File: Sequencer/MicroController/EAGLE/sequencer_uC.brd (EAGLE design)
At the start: 70 x 70 mm, 29 parts, among them J1 AVR_SPI_PROG_3X2NS, Q1 16MHz

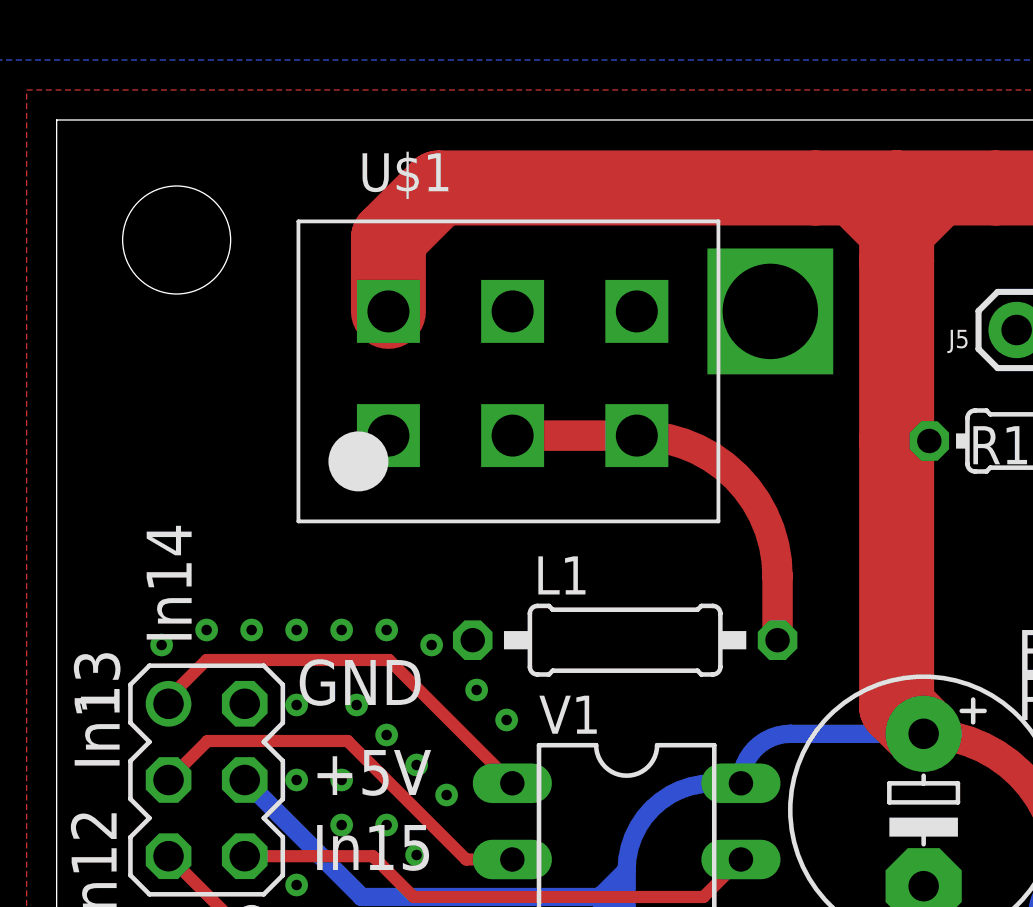
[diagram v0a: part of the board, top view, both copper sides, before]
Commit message: fixed TE pinout
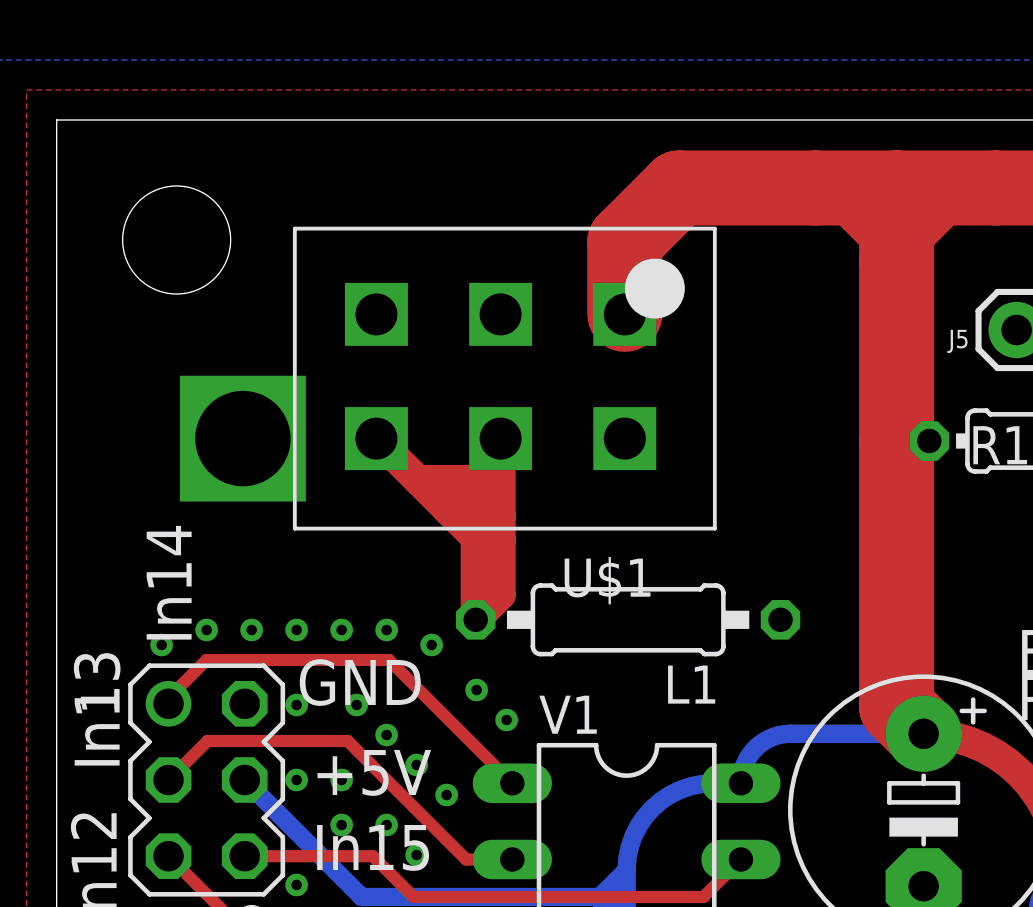
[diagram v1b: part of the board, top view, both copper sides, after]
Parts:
- moved U$1 8.95 mm to (18.9, 59.4), turned to 180 degrees
- moved L1 0.69 mm to (19.1, 53.3), turned to 180 degrees
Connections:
- net +5V: now also U$1.NULL
- net DGND: no longer U$1.NULL
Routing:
- net AGND: track 12.9 -> 22.7 mm
- net +5V: track 314.2 -> 306.4 mm
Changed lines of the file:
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@@
 <?xml version="1.0" encoding="utf-8"?>
 <!DOCTYPE eagle SYSTEM "eagle.dtd">
-<eagle version="9.3.1">
+<eagle version="9.2.2">
 <drawing>
 <settings>
@@
 <attribute name="VALUE" x="52.46" y="35.079" size="1.27" layer="27" ratio="10"/>
 </element>
-<element name="L1" library="rcl" library_urn="urn:adsk.eagle:library:334" package="0207/10" package3d_urn="urn:adsk.eagle:package:23491/2" value="47uH" x="18.95" y="52.66" smashed="yes">
-<attribute name="NAME" x="15.902" y="54.184" size="1.27" layer="25" ratio="10"/>
-<attribute name="SPICEPREFIX" value="L" x="38" y="-21" size="1.778" layer="27" display="off"/>
-<attribute name="VALUE" x="16.6894" y="52.025" size="1.27" layer="27" ratio="10"/>
+<element name="L1" library="rcl" library_urn="urn:adsk.eagle:library:334" package="0207/10" package3d_urn="urn:adsk.eagle:package:23491/1" value="47uH" x="19.05" y="53.34" smashed="yes" rot="R180">
+<attribute name="NAME" x="22.098" y="51.816" size="1.27" layer="25" ratio="10" rot="R180"/>
+<attribute name="SPICEPREFIX" value="L" x="0" y="127" size="1.778" layer="27" rot="R180" display="off"/>
+<attribute name="VALUE" x="21.3106" y="53.975" size="1.27" layer="27" ratio="10" rot="R180"/>
 </element>
 <element name="Q1" library="special" library_urn="urn:adsk.eagle:library:367" package="QS" package3d_urn="urn:adsk.eagle:package:26647/2" value="16MHz" x="29" y="27" smashed="yes" rot="R90">
@@
 <attribute name="VALUE" x="31.78" y="34.137" size="1.27" layer="27" ratio="10" rot="R180"/>
 </element>
-<element name="R1" library="resistor" library_urn="urn:adsk.eagle:library:348" package="0204/7" package3d_urn="urn:adsk.eagle:package:23498/1" value="10k" x="32.9" y="59.3" smashed="yes" rot="R180">
+<element name="R1" library="resistor" library_urn="urn:adsk.eagle:library:348" package="0204/7" package3d_urn="urn:adsk.eagle:package:25945/1" value="10k" x="32.9" y="59.3" smashed="yes" rot="R180">
 <attribute name="NAME" x="32.491" y="59.795" size="1.27" layer="25" ratio="10" rot="R180"/>
 <attribute name="VALUE" x="35.475" y="59.7858" size="1.27" layer="27" ratio="10" rot="R180"/>
 </element>
-<element name="R2" library="rcl" library_urn="urn:adsk.eagle:library:334" package="0204/7" package3d_urn="urn:adsk.eagle:package:23498/2" value="10k" x="53" y="54" smashed="yes" rot="R90">
+<element name="R2" library="rcl" library_urn="urn:adsk.eagle:library:334" package="0204/7" package3d_urn="urn:adsk.eagle:package:23498/1" value="10k" x="53" y="54" smashed="yes" rot="R90">
 <attribute name="NAME" x="51.7046" y="51.46" size="0.9906" layer="25" ratio="10" rot="R90"/>
 <attribute name="SPICEPREFIX" value="R" x="126.66" y="84.48" size="1.778" layer="27" rot="R90" display="off"/>
 <attribute name="VALUE" x="55.4826" y="54.3744" size="0.9906" layer="27" ratio="10" rot="R90"/>
 </element>
-<element name="R3" library="rcl" library_urn="urn:adsk.eagle:library:334" package="0204/7" package3d_urn="urn:adsk.eagle:package:23498/2" value="10k" x="57" y="51" smashed="yes" rot="R90">
+<element name="R3" library="rcl" library_urn="urn:adsk.eagle:library:334" package="0204/7" package3d_urn="urn:adsk.eagle:package:23498/1" value="10k" x="57" y="51" smashed="yes" rot="R90">
 <attribute name="NAME" x="55.7046" y="48.46" size="0.9906" layer="25" ratio="10" rot="R90"/>
 <attribute name="SPICEPREFIX" value="R" x="130.66" y="91.64" size="1.778" layer="27" rot="R90" display="off"/>
 <attribute name="VALUE" x="59.4826" y="51.3744" size="0.9906" layer="27" ratio="10" rot="R90"/>
 </element>
-<element name="R4" library="rcl" library_urn="urn:adsk.eagle:library:334" package="0204/7" package3d_urn="urn:adsk.eagle:package:23498/2" value="10k" x="28.34" y="13.2" smashed="yes" rot="R90">
+<element name="R4" library="rcl" library_urn="urn:adsk.eagle:library:334" package="0204/7" package3d_urn="urn:adsk.eagle:package:23498/1" value="10k" x="28.34" y="13.2" smashed="yes" rot="R90">
 <attribute name="NAME" x="27.0446" y="10.66" size="0.9906" layer="25" ratio="10" rot="R90"/>
 <attribute name="SPICEPREFIX" value="R" x="102" y="64" size="1.778" layer="27" rot="R90" display="off"/>
@@
 <attribute name="VALUE" x="0.809" y="49.27" size="1.27" layer="27" ratio="10" rot="R270"/>
 </element>
-<element name="U$1" library="TE6Pin" package="CAPSTONE_1-770875-0" value="TER6PIN_VERT" x="11.06" y="63.62" smashed="yes">
-<attribute name="NAME" x="10.06" y="67.62" size="1.27" layer="25"/>
-</element>
-<element name="V1" library="74ttl-din" library_urn="urn:adsk.eagle:library:84" package="DIL16" package3d_urn="urn:adsk.eagle:package:922/2" value="74595N" x="19" y="39" smashed="yes" rot="R270">
+<element name="U$1" library="TE6Pin" package="CAPSTONE_1-770875-0" value="TER6PIN_VERT" x="18.94" y="59.38" smashed="yes" rot="R180">
+<attribute name="NAME" x="19.94" y="55.38" size="1.27" layer="25" rot="R180"/>
+</element>
+<element name="V1" library="74ttl-din" library_urn="urn:adsk.eagle:library:84" package="DIL16" package3d_urn="urn:adsk.eagle:package:1462/1" value="74595N" x="19" y="39" smashed="yes" rot="R270">
 <attribute name="NAME" x="16.079" y="49.541" size="1.27" layer="25" ratio="10"/>
 <attribute name="VALUE" x="18.365" y="46.493" size="1.27" layer="27" ratio="10" rot="R270"/>
 </element>
-<element name="V2" library="74ttl-din" library_urn="urn:adsk.eagle:library:84" package="DIL16" package3d_urn="urn:adsk.eagle:package:922/2" value="74595N" x="19" y="16" smashed="yes" rot="R270">
+<element name="V2" library="74ttl-din" library_urn="urn:adsk.eagle:library:84" package="DIL16" package3d_urn="urn:adsk.eagle:package:1462/1" value="74595N" x="19" y="16" smashed="yes" rot="R270">
 <attribute name="NAME" x="16.079" y="26.541" size="1.27" layer="25" ratio="10"/>
 <attribute name="VALUE" x="18.365" y="23.493" size="1.27" layer="27" ratio="10" rot="R270"/>
@@
 <signals>
 <signal name="+5V">
-<contactref element="U$1" pad="+5V"/>
 <contactref element="C1" pad="+"/>
 <contactref element="C2" pad="1"/>
@@
 <contactref element="SV1" pad="4"/>
 <contactref element="SV1" pad="6"/>
-<wire x1="11.06" y1="63.62" x2="11.06" y2="66.06" width="2.5" layer="1"/>
-<wire x1="11.06" y1="66.06" x2="12.734" y2="67.734" width="2.5" layer="1"/>
-<wire x1="12.734" y1="67.734" x2="25.3" y2="67.734" width="2.5" layer="1"/>
+<wire x1="20.734" y1="67.734" x2="25.3" y2="67.734" width="2.5" layer="1"/>
 <wire x1="25.3" y1="67.734" x2="28" y2="67.734" width="2.5" layer="1"/>
 <wire x1="28" y1="67.734" x2="31.3" y2="67.734" width="2.5" layer="1"/>
@@
 <wire x1="50" y1="1.524" x2="51.45" y2="2.974" width="1.016" layer="1"/>
 <wire x1="51.45" y1="2.974" x2="51.45" y2="3" width="1.016" layer="1"/>
+<contactref element="U$1" pad="NULL"/>
+<contactref element="U$1" pad="+5V"/>
+<wire x1="18.94" y1="63.52" x2="18.94" y2="65.94" width="2.5" layer="1"/>
+<wire x1="18.94" y1="65.94" x2="20.734" y2="67.734" width="2.5" layer="1"/>
+<wire x1="6.27" y1="48" x2="6.21" y2="59.38" width="0" layer="19" extent="1-1"/>
 </signal>
 <signal name="DGND">
-<contactref element="U$1" pad="DGND"/>
-<contactref element="U$1" pad="NULL"/>
 <contactref element="C1" pad="-"/>
 <contactref element="C2" pad="2"/>
@@
 <via x="11" y="10.5" extent="1-16" drill="0.35"/>
 <via x="13" y="10.5" extent="1-16" drill="0.35"/>
+<contactref element="U$1" pad="DGND"/>
 </signal>
 <signal name="AGND">
+<contactref element="L1" pad="2"/>
+<contactref element="U$1" pad="AGND0"/>
 <contactref element="U$1" pad="AGND1"/>
-<contactref element="U$1" pad="AGND0"/>
-<contactref element="L1" pad="2"/>
-<wire x1="24.03" y1="52.66" x2="24.03" y2="54.79" width="1.016" layer="1"/>
-<wire x1="24.03" y1="54.79" x2="19.34" y2="59.48" width="1.016" layer="1" curve="90"/>
-<wire x1="19.34" y1="59.48" x2="15.2" y2="59.48" width="1.016" layer="1"/>
+<wire x1="13.97" y1="53.34" x2="13.97" y2="56.07" width="1" layer="1"/>
+<wire x1="13.97" y1="56.07" x2="13.24" y2="56.8" width="1" layer="1"/>
+<wire x1="13.02" y1="57.02" x2="12.04" y2="58" width="1" layer="1"/>
+<wire x1="12.02" y1="58.02" x2="10.66" y2="59.38" width="1" layer="1"/>
+<wire x1="13.97" y1="53.34" x2="14.8" y2="54.17" width="1" layer="1"/>
+<wire x1="14.8" y1="54.17" x2="14.8" y2="56" width="1" layer="1"/>
+<wire x1="14.8" y1="56" x2="14.8" y2="56.8" width="1" layer="1"/>
+<wire x1="14.8" y1="56.8" x2="14.8" y2="59.38" width="1" layer="1"/>
+<wire x1="13.02" y1="57.02" x2="13.24" y2="56.8" width="1" layer="1"/>
+<wire x1="13.24" y1="56.8" x2="14.8" y2="56.8" width="1" layer="1"/>
+<wire x1="13.02" y1="57.02" x2="14" y2="58" width="1" layer="1"/>
+<wire x1="14" y1="58" x2="14.8" y2="58.8" width="1" layer="1"/>
+<wire x1="14.8" y1="58.8" x2="14.8" y2="59.38" width="1" layer="1"/>
+<wire x1="14.8" y1="56" x2="14" y2="56.8" width="1" layer="1"/>
+<wire x1="14" y1="56.8" x2="14" y2="58" width="1" layer="1"/>
+<wire x1="14" y1="58" x2="12.04" y2="58" width="1" layer="1"/>
+<wire x1="12.04" y1="58" x2="12.02" y2="58.02" width="1" layer="1"/>
 </signal>
 <signal name="N$1">

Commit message: cleanup
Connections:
- net +5V: no longer U$1.NULL
- net DGND: now also U$1.NULL
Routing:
- net RESET: track 42.9 -> 46.5 mm
- net ~EN: track 32.5 -> 31.2 mm
- net +5V: track 306.4 -> 305.4 mm
- net MOSI: track 14.7 -> 14.0 mm
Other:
- board text added: "Sequencer Koltin Kosik-Harvey March 7 / 2019"
- board text removed: "Sequencer Koltin Kosik-Harvey March 3 / 2019"
